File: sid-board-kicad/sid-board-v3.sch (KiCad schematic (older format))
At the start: 49 parts, among them J1 SPI + UART, J2 USB_B_Micro, J3 Conn_01x12, Q1 BSS138, Q2 BSS138, SW1 SW_EN, SW2 SW_FLASH, U1 SC16IS752IPW, U2 MCP1703A-3302_SOT223, U3 SN65HVD232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

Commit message: Labelling and reorganisation
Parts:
- J3: value Conn_01x12 -> Conn_01x08; footprint Connector_PinHeader_2.54mm:PinHeader_1x12_P2.54mm_Vertical -> Connector_PinHeader_2.54mm:PinHeader_1x08_P2.54mm_Vertical; symbol Connector_Generic:Conn_01x12 -> Connector_Generic:Conn_01x08
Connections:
- net labels added: I2S_BCLK, I2S_DIN, I2S_WSEL
- wire segments 84 -> 71
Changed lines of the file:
@@
 $EndComp
 $Comp
-L Connector_Generic:Conn_01x12 J3
+L Connector_Generic:Conn_01x08 J3
 U 1 1 5F374BE1
-P 5500 7050
-F 0 "J3" V 5625 6996 50  0000 C CNN
-F 1 "Conn_01x12" V 5716 6996 50  0000 C CNN
-F 2 "Connector_PinHeader_2.54mm:PinHeader_1x12_P2.54mm_Vertical" H 5500 7050 50  0001 C CNN
-F 3 "~" H 5500 7050 50  0001 C CNN
-	1    5500 7050
+P 5400 7350
+F 0 "J3" V 5525 7296 50  0000 C CNN
+F 1 "Conn_01x08" V 5616 7296 50  0000 C CNN
+F 2 "Connector_PinHeader_2.54mm:PinHeader_1x08_P2.54mm_Vertical" H 5400 7350 50  0001 C CNN
+F 3 "~" H 5400 7350 50  0001 C CNN
+	1    5400 7350
 	0    1    1    0
 $EndComp
-Text GLabel 5900 6850 1    50   Input ~ 0
+Text GLabel 5600 7150 1    50   Input ~ 0
 VDD_3.3V
-Text GLabel 6000 6850 1    50   Input ~ 0
+Text GLabel 5700 7150 1    50   Input ~ 0
 GND
 Wire Wire Line
 	4700 4050 5700 4050
 Wire Wire Line
-	5700 4050 5700 6850
+	4700 4150 5600 4150
+Text GLabel 5900 5350 2    50   Input ~ 0
+I2S_DIN
+Text GLabel 5900 5550 2    50   Input ~ 0
+I2S_WSEL
+Text GLabel 5900 5650 2    50   Input ~ 0
+I2S_BCLK
+Text GLabel 5200 7150 1    50   Input ~ 0
+I2S_DIN
+Text GLabel 5100 7150 1    50   Input ~ 0
+I2S_WSEL
+Text GLabel 5000 7150 1    50   Input ~ 0
+I2S_BCLK
 Wire Wire Line
-	4700 4150 5600 4150
+	5900 5950 5400 5950
 Wire Wire Line
-	5600 4150 5600 6850
+	5400 5950 5400 7150
 Wire Wire Line
-	5900 6050 5500 6050
+	5900 5850 5500 5850
 Wire Wire Line
-	5500 6050 5500 6850
+	5500 5850 5500 7150
 Wire Wire Line
-	5900 6150 5400 6150
+	5900 5750 5350 5750
 Wire Wire Line
-	5400 6150 5400 6850
+	5350 5750 5350 7150
 Wire Wire Line
-	5900 5850 5200 5850
-Wire Wire Line
-	5200 5850 5200 6600
-Wire Wire Line
-	5200 6600 5300 6600
-Wire Wire Line
-	5300 6600 5300 6850
-Wire Wire Line
-	5900 5950 5250 5950
-Wire Wire Line
-	5250 5950 5250 6750
-Wire Wire Line
-	5250 6750 5200 6750
-Wire Wire Line
-	5200 6750 5200 6850
-Wire Wire Line
-	5900 5550 5100 5550
-Wire Wire Line
-	5100 5550 5100 6850
-Wire Wire Line
-	5900 5650 5000 5650
-Wire Wire Line
-	5000 5650 5000 6850
-Wire Wire Line
-	5900 5750 4900 5750
-Wire Wire Line
-	4900 5750 4900 6850
+	5350 7150 5300 7150
+Wire Notes Line
+	4850 6650 5850 6650
+Wire Notes Line
+	5850 6650 5850 7650
+Wire Notes Line
+	5850 7650 4850 7650
+Wire Notes Line
+	4850 7650 4850 6650
 $EndSCHEMATC

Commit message: Lost labelling. Moved debug header.
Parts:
- J1: footprint Connector_PinHeader_1.00mm:PinHeader_2x05_P1.00mm_Vertical -> Connector_PinHeader_2.00mm:PinHeader_2x05_P2.00mm_Vertical
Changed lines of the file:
@@
 F 0 "J1" H 10000 6217 50  0000 C CNN
 F 1 "SPI + UART" H 10000 6126 50  0000 C CNN
-F 2 "Connector_PinHeader_1.00mm:PinHeader_2x05_P1.00mm_Vertical" H 9950 5900 50  0001 C CNN
+F 2 "Connector_PinHeader_2.00mm:PinHeader_2x05_P2.00mm_Vertical" H 9950 5900 50  0001 C CNN
 F 3 "~" H 9950 5900 50  0001 C CNN
 	1    9950 5900

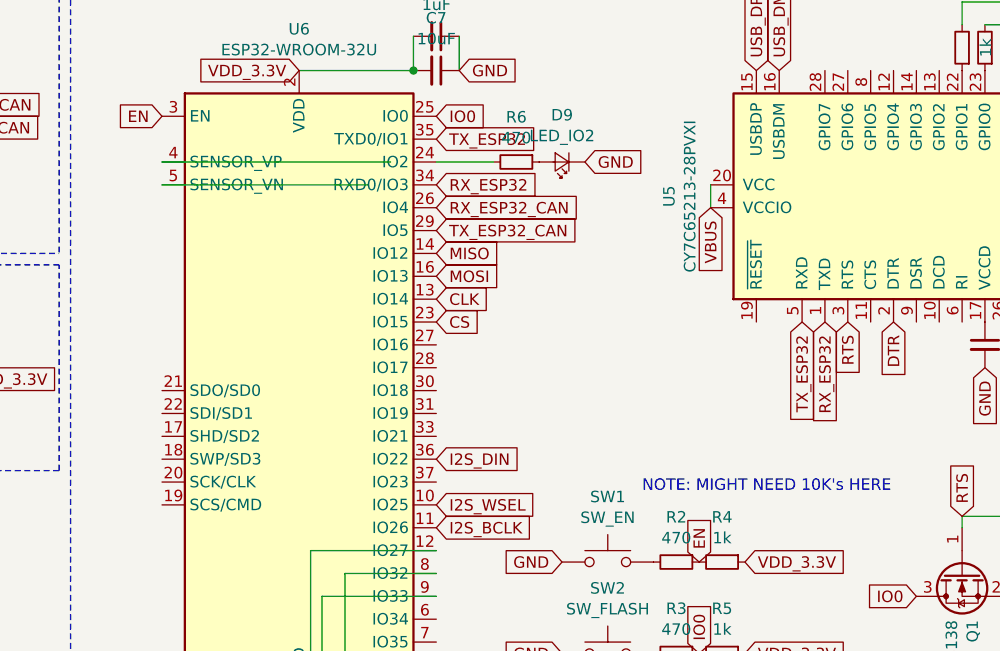
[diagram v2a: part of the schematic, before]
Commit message: Checked bootstrapping pins. Checked RX TX pins.
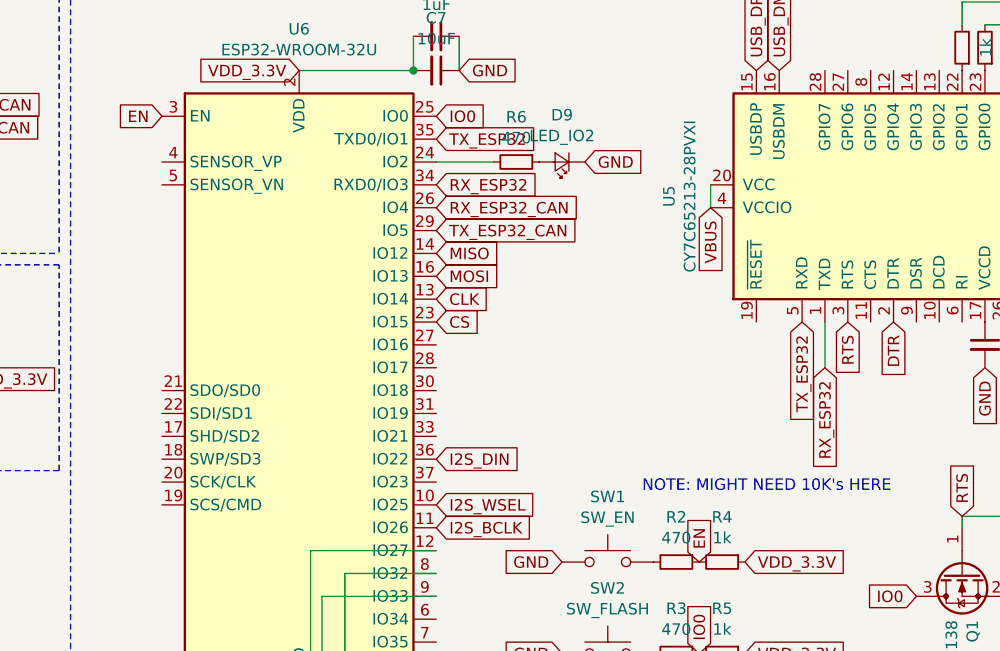
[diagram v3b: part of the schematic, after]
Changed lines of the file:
@@
 Wire Notes Line
 	4300 850  4300 2800
-Text GLabel 7600 4750 3    50   Input ~ 0
-RX_ESP32
 Text GLabel 5900 4150 2    50   Input ~ 0
 RX_ESP32
@@
 Text GLabel 5700 7150 1    50   Input ~ 0
 GND
-Wire Wire Line
-	4700 4050 5700 4050
-Wire Wire Line
-	4700 4150 5600 4150
 Text GLabel 5900 5350 2    50   Input ~ 0
 I2S_DIN
@@
 Wire Notes Line
 	4850 7650 4850 6650
+Text GLabel 7600 4950 3    50   Input ~ 0
+RX_ESP32
+Wire Wire Line
+	7600 4950 7600 4750
 $EndSCHEMATC

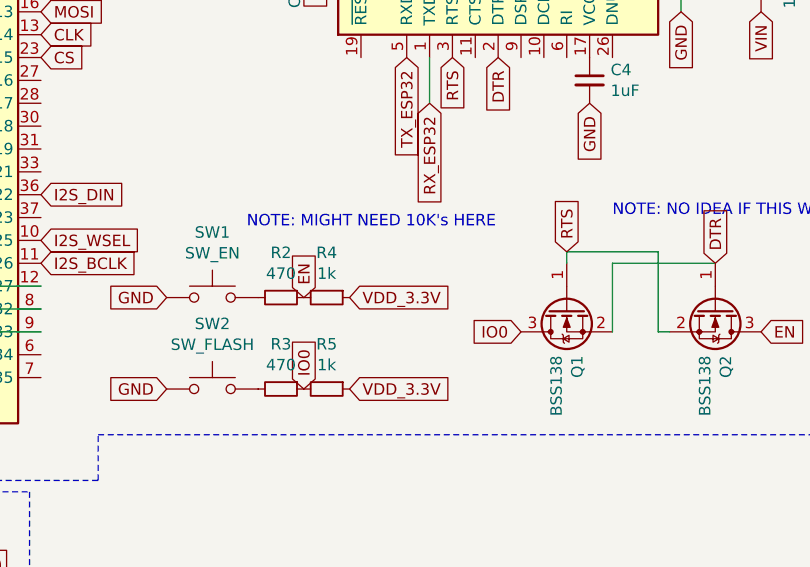
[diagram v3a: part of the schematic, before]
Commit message: Added 10ks
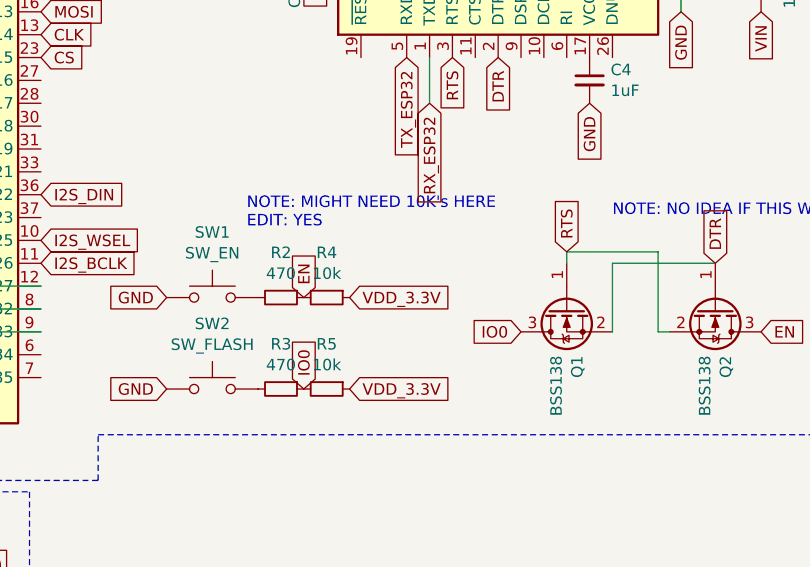
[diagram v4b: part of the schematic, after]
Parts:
- R4, R5: value 1k -> 10k
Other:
- note added: "NOTE: MIGHT NEED 10K's HERE\nEDIT: YES"
- note removed: "NOTE: MIGHT NEED 10K's HERE"
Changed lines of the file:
@@
 P 7150 5800
 F 0 "R4" V 6954 5800 50  0000 C CNN
-F 1 "1k" V 7045 5800 50  0000 C CNN
+F 1 "10k" V 7045 5800 50  0000 C CNN
 F 2 "Resistor_SMD:R_0805_2012Metric_Pad1.15x1.40mm_HandSolder" H 7150 5800 50  0001 C CNN
 F 3 "~" H 7150 5800 50  0001 C CNN
@@
 P 7150 6200
 F 0 "R5" V 6954 6200 50  0000 C CNN
-F 1 "1k" V 7045 6200 50  0000 C CNN
+F 1 "10k" V 7045 6200 50  0000 C CNN
 F 2 "Resistor_SMD:R_0805_2012Metric_Pad1.15x1.40mm_HandSolder" H 7150 6200 50  0001 C CNN
 F 3 "~" H 7150 6200 50  0001 C CNN
@@
 VDD_3.3V
 Text Notes 6800 5500 0    50   ~ 0
-NOTE: MIGHT NEED 10K's HERE
+NOTE: MIGHT NEED 10K's HERE\nEDIT: YES
 Text Notes 8400 5450 0    50   ~ 0
 NOTE: NO IDEA IF THIS WILL WORK LMAO
